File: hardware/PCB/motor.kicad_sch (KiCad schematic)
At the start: 44 parts

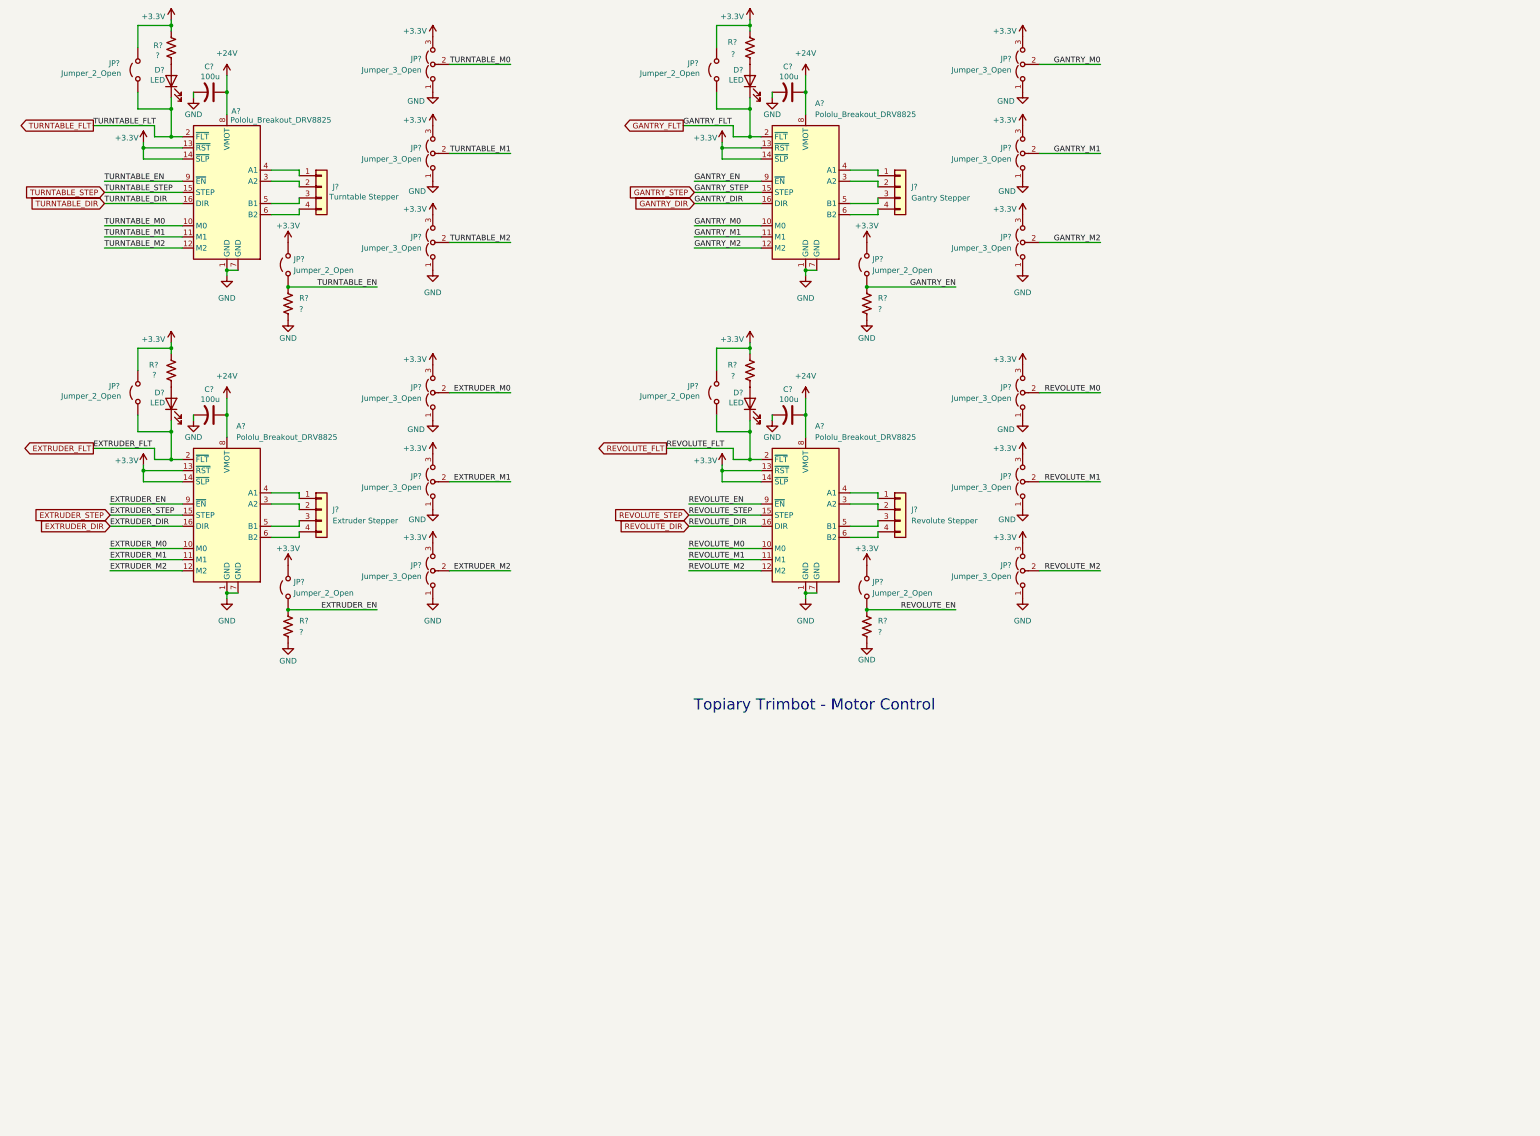
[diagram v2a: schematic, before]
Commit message: Add more symbols and continue filling footprints
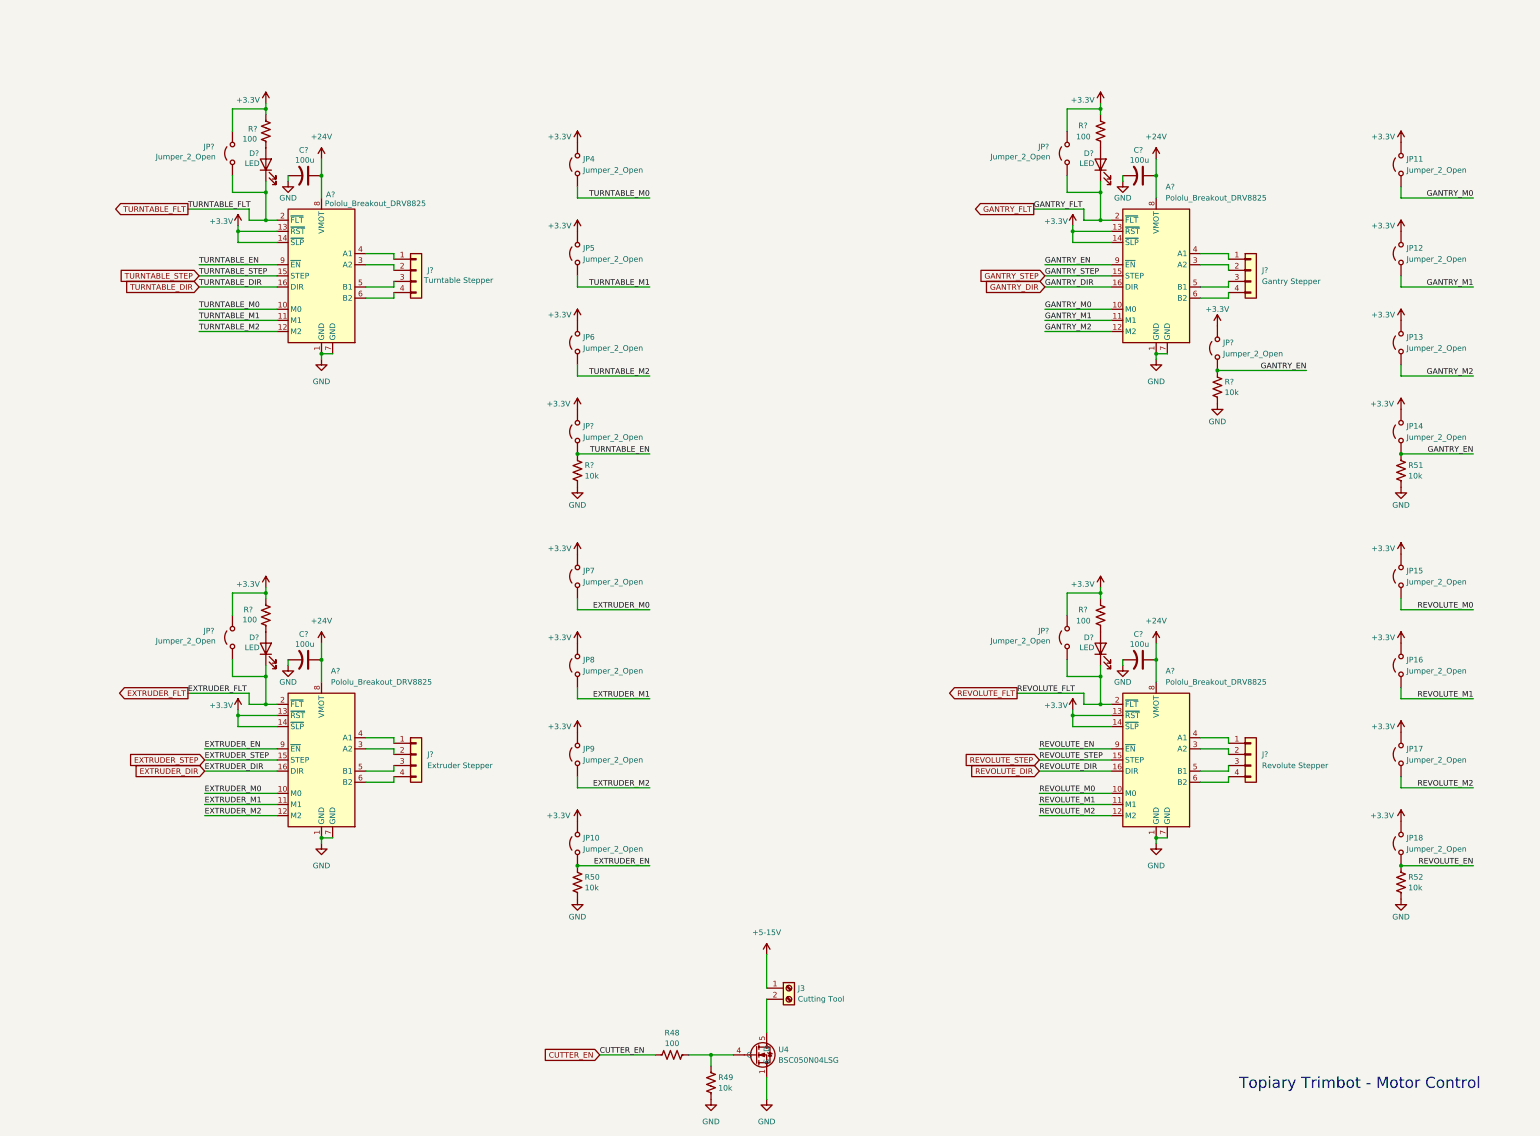
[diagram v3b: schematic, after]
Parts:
- removed JP? (x12): Jumper_3_Open, Connector_PinHeader_1.00mm:PinHeader_1x03_P1.00mm_Vertical, symbol Jumper:Jumper_3_Open
- removed JP? (x2): Jumper_2_Open, Connector_PinHeader_1.00mm:PinHeader_1x02_P1.00mm_Vertical, symbol Jumper:Jumper_2_Open
- removed R? (x2): ?, Resistor_SMD:R_0805_2012Metric, symbol Device:R_US
- added J3: Cutting Tool, CustomFootprints:6DBL-02-006, symbol Connector:Screw_Terminal_01x02
- added JP10, JP11, JP12, JP13, JP14, JP15, JP16, JP17, JP18, JP4, JP5, JP6, JP7, JP8, JP9: Jumper_2_Open, Connector_PinHeader_1.00mm:PinHeader_1x02_P1.00mm_Vertical, symbol Jumper:Jumper_2_Open
- added R48: 100, Resistor_SMD:R_0805_2012Metric, symbol Device:R_US
- added R49, R50, R51, R52: 10k, Resistor_SMD:R_0805_2012Metric, symbol Device:R_US
- added U4: BSC050N04LSG, Package_TO_SOT_SMD:TDSON-8-1, symbol CustomSymbols:BSC050N04LSG
- D? (x4): footprint (none) -> LED_SMD:LED_0805_2012Metric
- J? (x4): footprint (none) -> Connector_Molex:Molex_KK-254_AE-6410-04A_1x04_P2.54mm_Vertical
- R? (x4): value ? -> 100
- R? (x2): value ? -> 10k
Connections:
- net +3.3V: now also JP10.2 (B), JP11.2 (B), JP12.2 (B), JP13.2 (B), JP14.2 (B), JP15.2 (B), JP16.2 (B), JP17.2 (B), JP18.2 (B), JP4.2 (B), JP5.2 (B), JP6.2 (B), JP7.2 (B), JP8.2 (B), JP9.2 (B)
- net EXTRUDER_EN: now also JP10.1 (A), R50.1
- net EXTRUDER_M0: now also JP7.1 (A)
- net EXTRUDER_M1: now also JP8.1 (A)
- net EXTRUDER_M2: now also JP9.1 (A)
- net GANTRY_EN: now also JP14.1 (A), R51.1
- net GANTRY_M0: now also JP11.1 (A)
- net GANTRY_M1: now also JP12.1 (A)
- net GANTRY_M2: now also JP13.1 (A)
- net GND: now also R49.1, R50.2, R51.2, R52.2, U4.1 (S), U4.2 (S), U4.3 (S)
- net REVOLUTE_EN: now also JP18.1 (A), R52.1
- net REVOLUTE_M0: now also JP15.1 (A)
- net REVOLUTE_M1: now also JP16.1 (A)
- net REVOLUTE_M2: now also JP17.1 (A)
- net TURNTABLE_M0: now also JP4.1 (A)
- net TURNTABLE_M1: now also JP5.1 (A)
- net TURNTABLE_M2: now also JP6.1 (A)
- new net: R48.2, R49.2, U4.4 (G)
- new net: J3.2 (Pin_2), U4.5 (D)
- new net +5-15V: J3.1 (Pin_1)
- new net CUTTER_EN: R48.1
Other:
- moved on the sheet: A?, C?, D?, J?, JP?, R?

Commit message: Finished setting footprints for LCD, motors, RPi, and storage schematics
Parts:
- JP10, JP11, JP12, JP13, JP14, JP15, JP16, JP17, JP18, JP4, JP5, JP6, JP7, JP8, JP9, JP? (x6): footprint Connector_PinHeader_1.00mm:PinHeader_1x02_P1.00mm_Vertical -> Connector_PinHeader_2.54mm:PinHeader_1x02_P2.54mm_Vertical
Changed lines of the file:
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@@
 			)
 		)
-		(property "Footprint" "Connector_PinHeader_1.00mm:PinHeader_1x02_P1.00mm_Vertical"
+		(property "Footprint" "Connector_PinHeader_2.54mm:PinHeader_1x02_P2.54mm_Vertical"
 			(at 160.02 144.78 0)
 			(effects
@@
 			)
 		)
-		(property "Footprint" "Connector_PinHeader_1.00mm:PinHeader_1x02_P1.00mm_Vertical"
+		(property "Footprint" "Connector_PinHeader_2.54mm:PinHeader_1x02_P2.54mm_Vertical"
 			(at 160.02 50.8 0)
 			(effects
@@
 			)
 		)
-		(property "Footprint" "Connector_PinHeader_1.00mm:PinHeader_1x02_P1.00mm_Vertical"
+		(property "Footprint" "Connector_PinHeader_2.54mm:PinHeader_1x02_P2.54mm_Vertical"
 			(at 160.02 165.1 0)
 			(effects
@@
 			)
 		)
-		(property "Footprint" "Connector_PinHeader_1.00mm:PinHeader_1x02_P1.00mm_Vertical"
+		(property "Footprint" "Connector_PinHeader_2.54mm:PinHeader_1x02_P2.54mm_Vertical"
 			(at 81.28 158.75 0)
 			(effects
@@
 			)
 		)
-		(property "Footprint" "Connector_PinHeader_1.00mm:PinHeader_1x02_P1.00mm_Vertical"
+		(property "Footprint" "Connector_PinHeader_2.54mm:PinHeader_1x02_P2.54mm_Vertical"
 			(at 347.98 111.76 0)
 			(effects
@@
 			)
 		)
-		(property "Footprint" "Connector_PinHeader_1.00mm:PinHeader_1x02_P1.00mm_Vertical"
+		(property "Footprint" "Connector_PinHeader_2.54mm:PinHeader_1x02_P2.54mm_Vertical"
 			(at 347.98 144.78 0)
 			(effects
@@
 			)
 		)
-		(property "Footprint" "Connector_PinHeader_1.00mm:PinHeader_1x02_P1.00mm_Vertical"
+		(property "Footprint" "Connector_PinHeader_2.54mm:PinHeader_1x02_P2.54mm_Vertical"
 			(at 160.02 71.12 0)
 			(effects
@@
 			)
 		)
-		(property "Footprint" "Connector_PinHeader_1.00mm:PinHeader_1x02_P1.00mm_Vertical"
+		(property "Footprint" "Connector_PinHeader_2.54mm:PinHeader_1x02_P2.54mm_Vertical"
 			(at 306.07 92.71 0)
 			(effects
@@
 			)
 		)
-		(property "Footprint" "Connector_PinHeader_1.00mm:PinHeader_1x02_P1.00mm_Vertical"
+		(property "Footprint" "Connector_PinHeader_2.54mm:PinHeader_1x02_P2.54mm_Vertical"
 			(at 347.98 205.74 0)
 			(effects
@@
 			)
 		)
-		(property "Footprint" "Connector_PinHeader_1.00mm:PinHeader_1x02_P1.00mm_Vertical"
+		(property "Footprint" "Connector_PinHeader_2.54mm:PinHeader_1x02_P2.54mm_Vertical"
 			(at 160.02 91.44 0)
 			(effects
@@
 			)
 		)
-		(property "Footprint" "Connector_PinHeader_1.00mm:PinHeader_1x02_P1.00mm_Vertical"
+		(property "Footprint" "Connector_PinHeader_2.54mm:PinHeader_1x02_P2.54mm_Vertical"
 			(at 347.98 50.8 0)
 			(effects
@@
 			)
 		)
-		(property "Footprint" "Connector_PinHeader_1.00mm:PinHeader_1x02_P1.00mm_Vertical"
+		(property "Footprint" "Connector_PinHeader_2.54mm:PinHeader_1x02_P2.54mm_Vertical"
 			(at 160.02 205.74 0)
 			(effects
@@
 			)
 		)
-		(property "Footprint" "Connector_PinHeader_1.00mm:PinHeader_1x02_P1.00mm_Vertical"
+		(property "Footprint" "Connector_PinHeader_2.54mm:PinHeader_1x02_P2.54mm_Vertical"
 			(at 347.98 71.12 0)
 			(effects
@@
 			)
 		)
-		(property "Footprint" "Connector_PinHeader_1.00mm:PinHeader_1x02_P1.00mm_Vertical"
+		(property "Footprint" "Connector_PinHeader_2.54mm:PinHeader_1x02_P2.54mm_Vertical"
 			(at 271.78 48.26 0)
 			(effects
@@
 			)
 		)
-		(property "Footprint" "Connector_PinHeader_1.00mm:PinHeader_1x02_P1.00mm_Vertical"
+		(property "Footprint" "Connector_PinHeader_2.54mm:PinHeader_1x02_P2.54mm_Vertical"
 			(at 160.02 111.76 0)
 			(effects
@@
 			)
 		)
-		(property "Footprint" "Connector_PinHeader_1.00mm:PinHeader_1x02_P1.00mm_Vertical"
+		(property "Footprint" "Connector_PinHeader_2.54mm:PinHeader_1x02_P2.54mm_Vertical"
 			(at 347.98 185.42 0)
 			(effects
@@
 			)
 		)
-		(property "Footprint" "Connector_PinHeader_1.00mm:PinHeader_1x02_P1.00mm_Vertical"
+		(property "Footprint" "Connector_PinHeader_2.54mm:PinHeader_1x02_P2.54mm_Vertical"
 			(at 271.78 158.75 0)
 			(effects
@@
 			)
 		)
-		(property "Footprint" "Connector_PinHeader_1.00mm:PinHeader_1x02_P1.00mm_Vertical"
+		(property "Footprint" "Connector_PinHeader_2.54mm:PinHeader_1x02_P2.54mm_Vertical"
 			(at 160.02 185.42 0)
 			(effects
@@
 			)
 		)
-		(property "Footprint" "Connector_PinHeader_1.00mm:PinHeader_1x02_P1.00mm_Vertical"
+		(property "Footprint" "Connector_PinHeader_2.54mm:PinHeader_1x02_P2.54mm_Vertical"
 			(at 347.98 165.1 0)
 			(effects
@@
 			)
 		)
-		(property "Footprint" "Connector_PinHeader_1.00mm:PinHeader_1x02_P1.00mm_Vertical"
+		(property "Footprint" "Connector_PinHeader_2.54mm:PinHeader_1x02_P2.54mm_Vertical"
 			(at 81.28 48.26 0)
 			(effects
@@
 			)
 		)
-		(property "Footprint" "Connector_PinHeader_1.00mm:PinHeader_1x02_P1.00mm_Vertical"
+		(property "Footprint" "Connector_PinHeader_2.54mm:PinHeader_1x02_P2.54mm_Vertical"
 			(at 347.98 91.44 0)
 			(effects

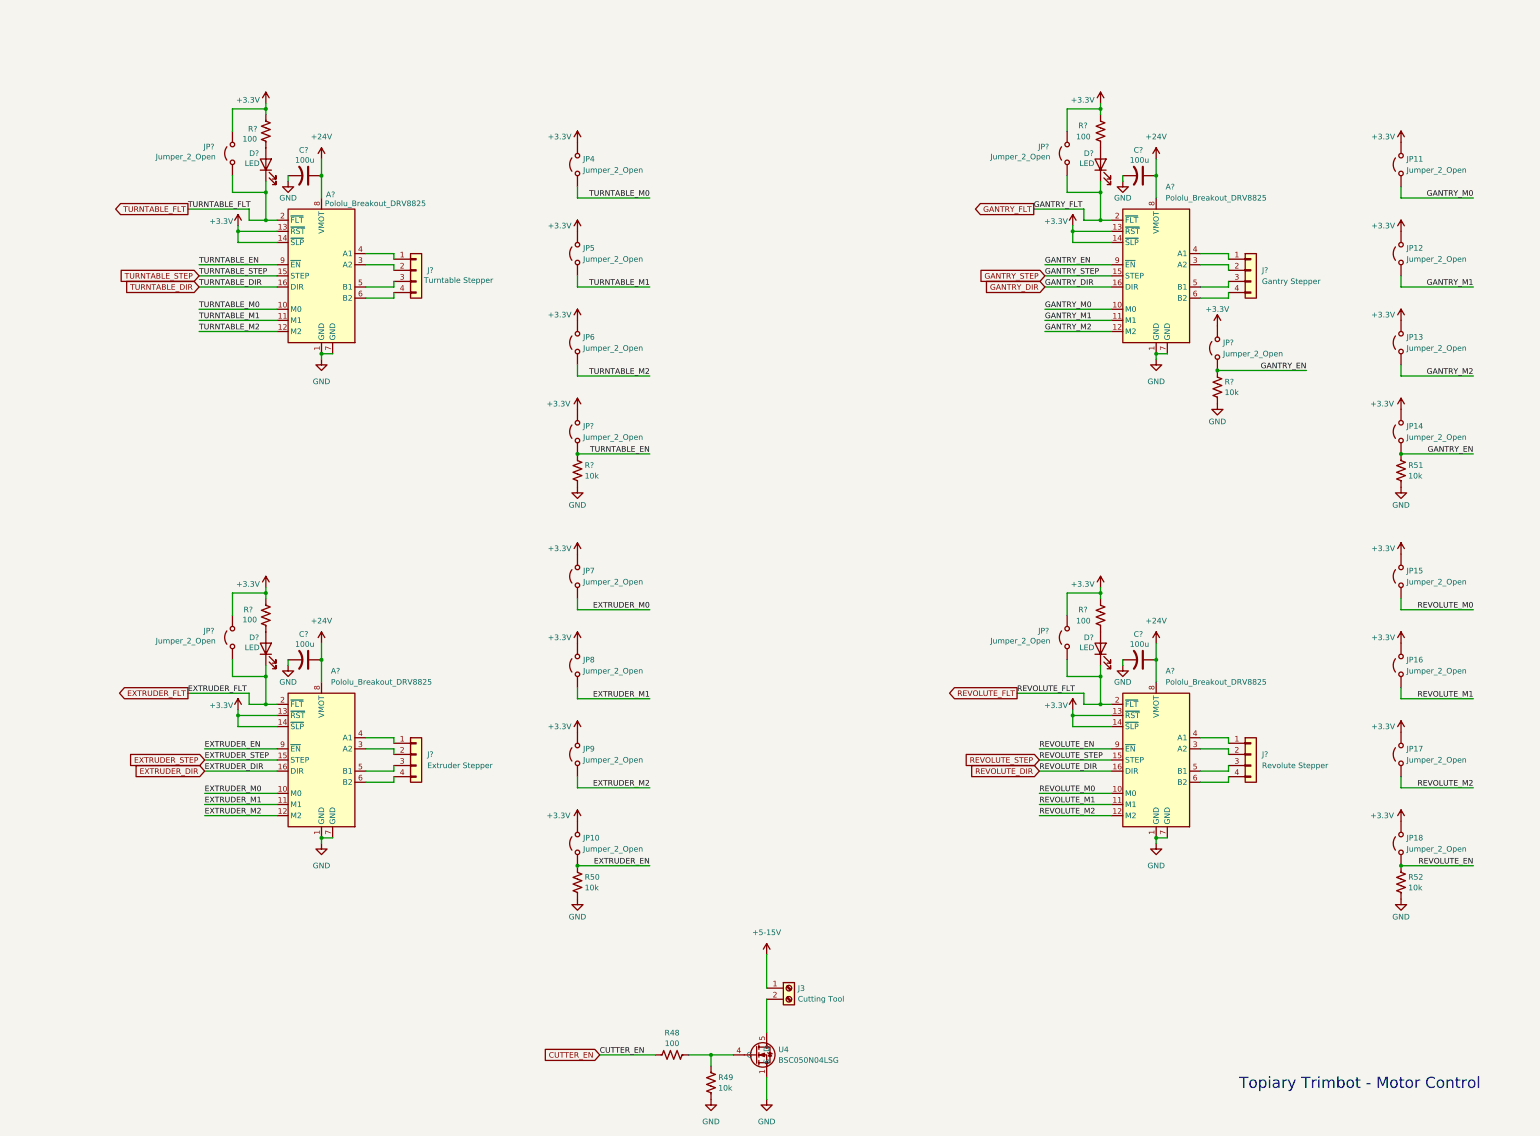
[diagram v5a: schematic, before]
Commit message: Schematic - Driver Fault LEDs
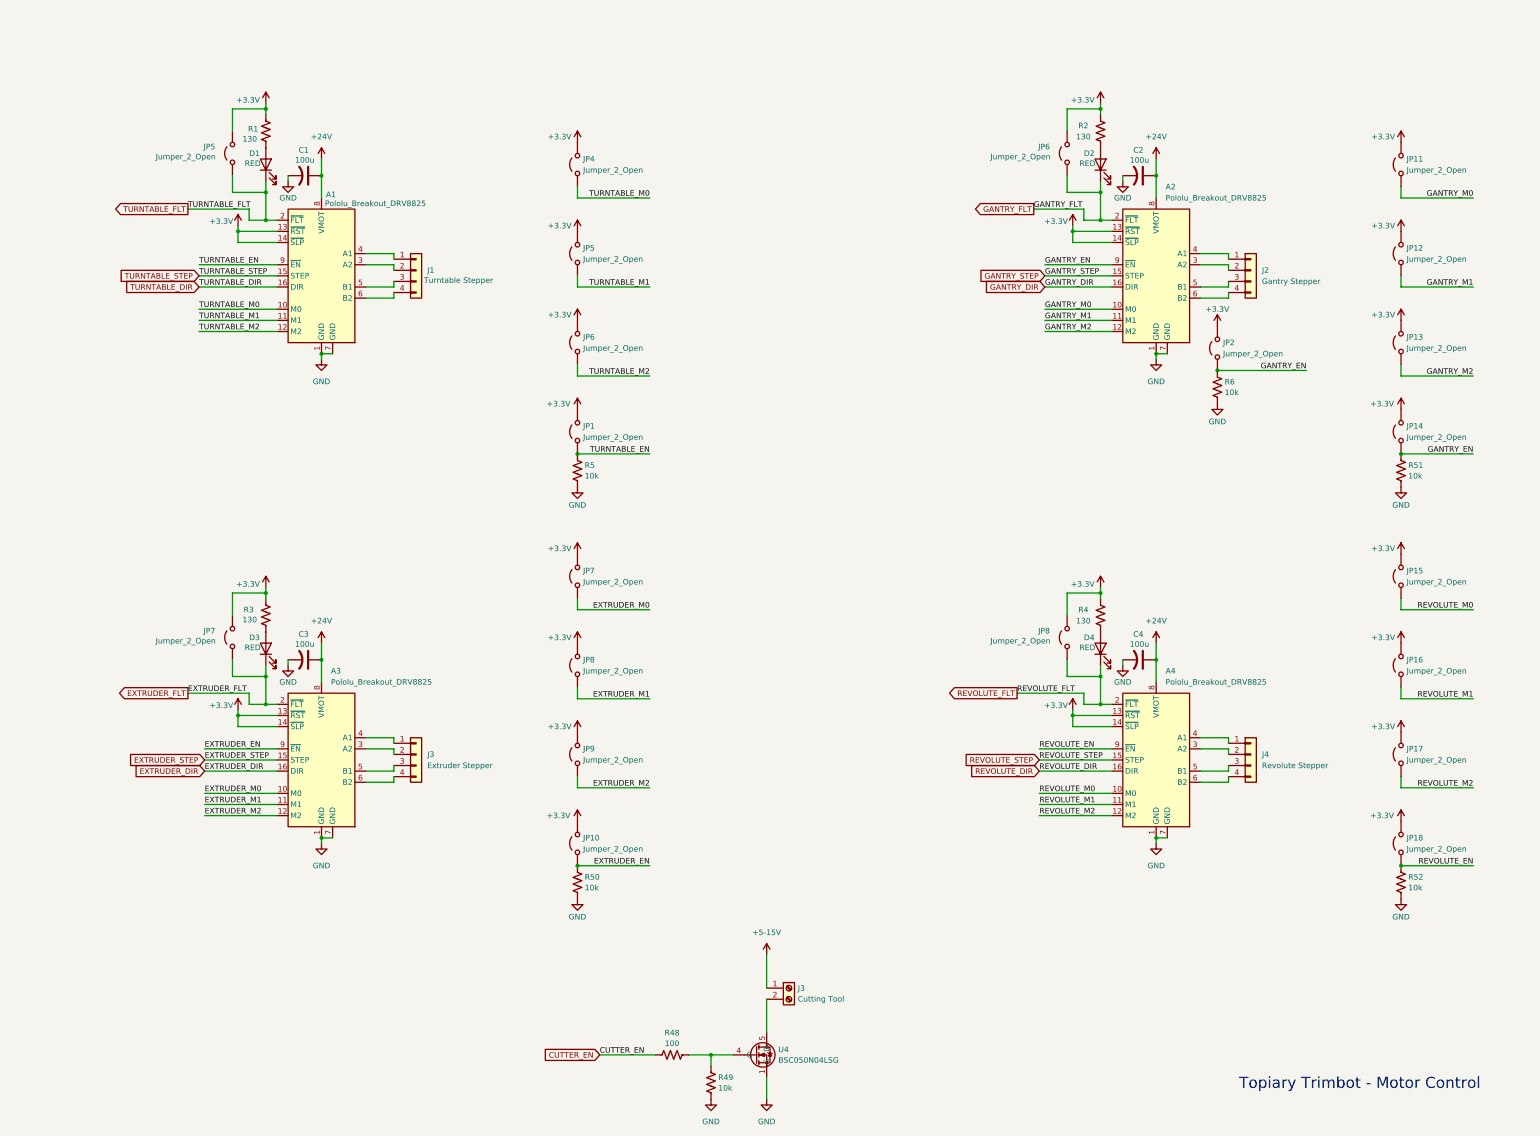
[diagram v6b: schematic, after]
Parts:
- D1, D2, D3, D4: renamed from D?; value LED -> RED
- R1, R2, R3, R4: renamed from R?; value 100 -> 130
- gave numbers to parts that had none: 20

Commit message: Schematic - Connector
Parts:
- renumbered A4 to A?, A3 to A?, A2 to A?, A1 to A?, C4 to C?, C3 to C?, C1 to C?, C2 to C?, D2 to D?, D3 to D?, D4 to D?, D1 to D?, J4 to J?, J1 to J?, J2 to J?, J3 to J?, JP7 to JP?, JP2 to JP?, JP6 to JP?, JP1 to JP?, JP8 to JP?, JP5 to JP?, R3 to R?, R5 to R?, R1 to R?, R4 to R?, R2 to R?, R6 to R?
